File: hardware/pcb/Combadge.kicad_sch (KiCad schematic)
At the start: 21 parts, among them J1 Conn_01x02_Socket, J2 Conn_01x01_Socket, J3 TOUCH, SW1 SW_Push, U1 ESP32-WROOM-32, U2 MAX98357AETE+T

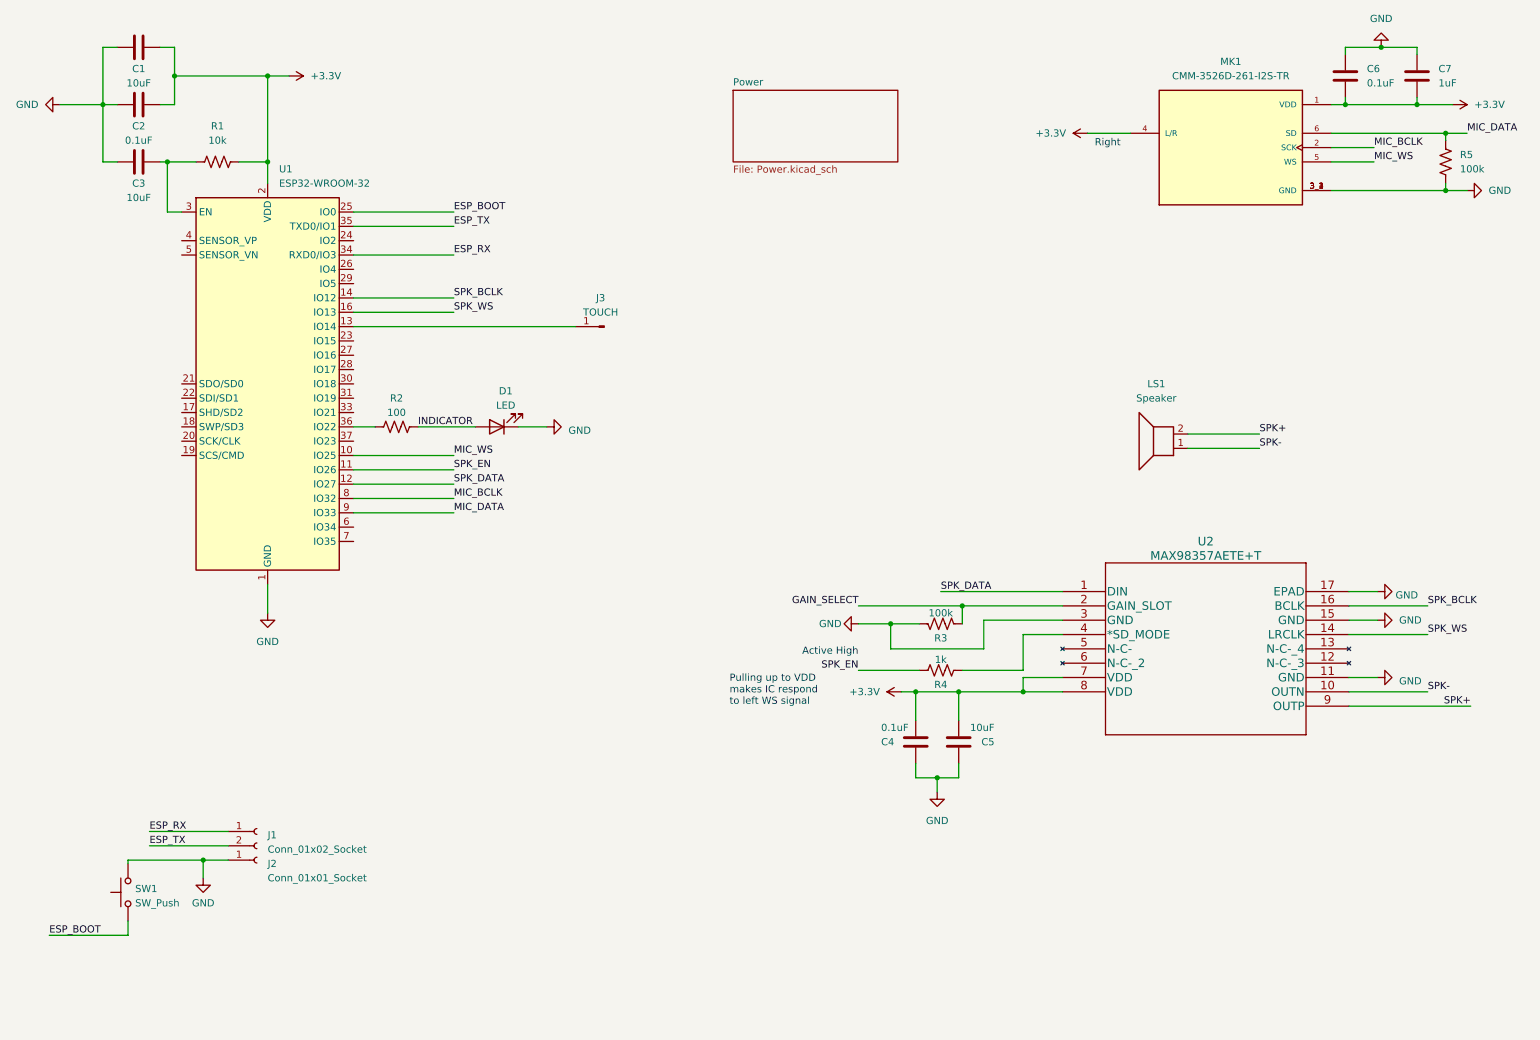
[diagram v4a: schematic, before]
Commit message: Cleanup schematic to follow convention
Thanks to Reddit users Crazy_Direction_1084 and AgentiMi for introducing
me to this.
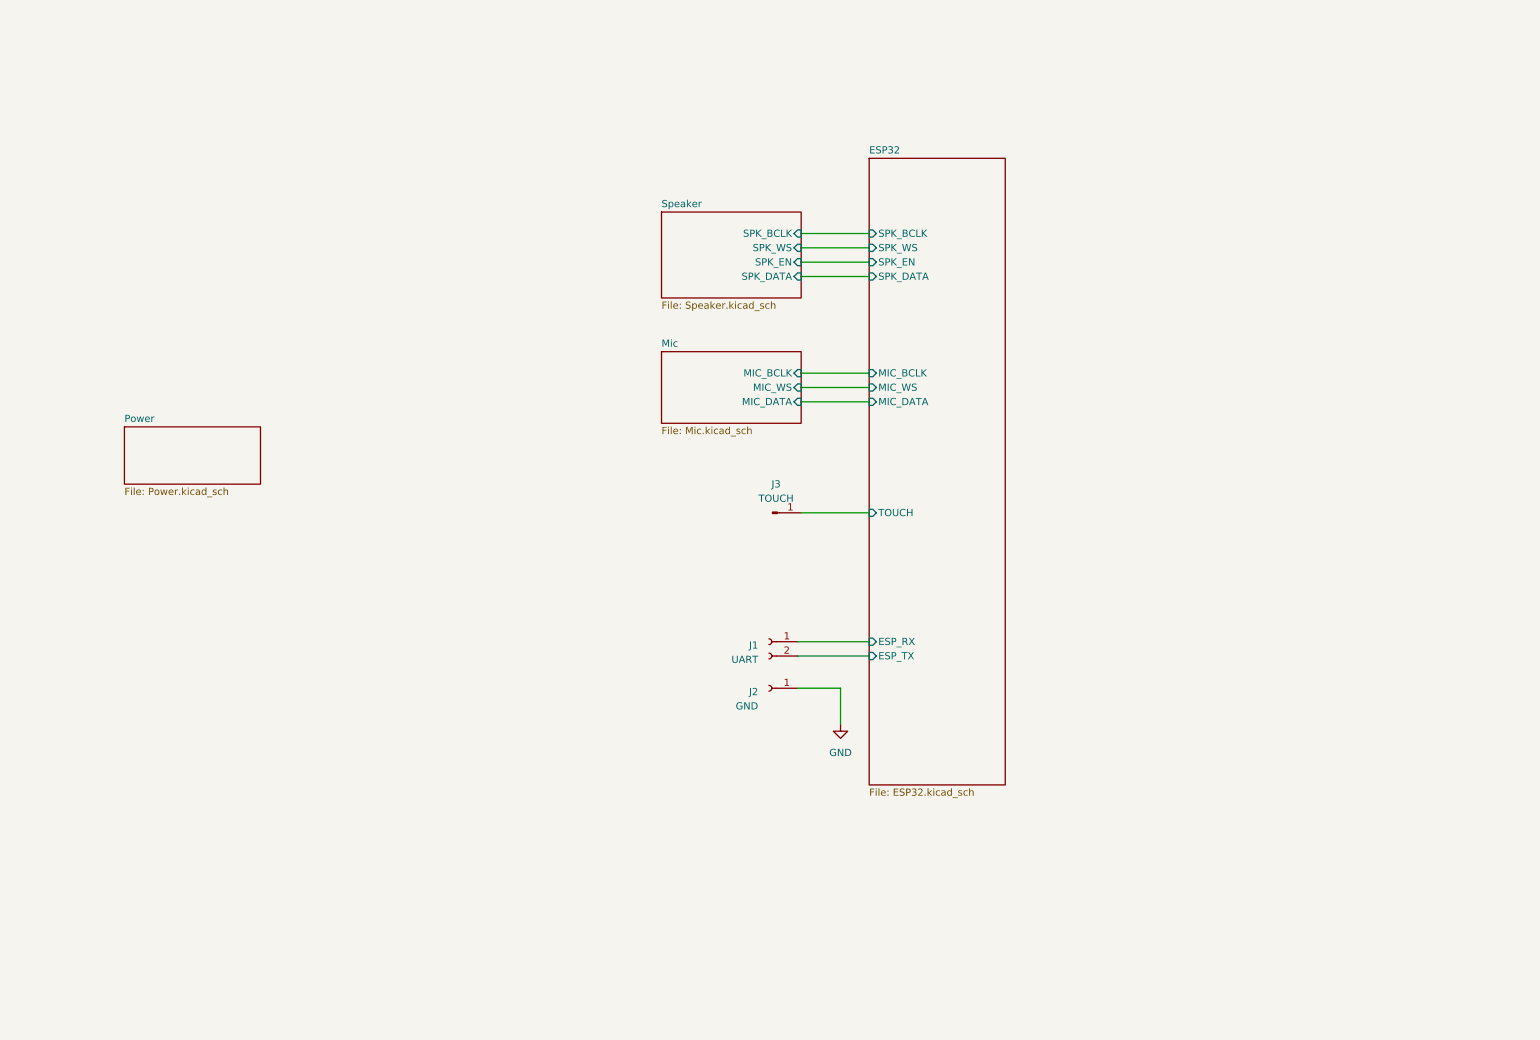
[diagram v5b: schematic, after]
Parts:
- removed C1, C3, C5: 10uF, Capacitor_SMD:C_1206_3216Metric_Pad1.33x1.80mm_HandSolder, symbol Device:C
- removed C2, C4, C6: 0.1uF, Capacitor_SMD:C_1206_3216Metric_Pad1.33x1.80mm_HandSolder, symbol Device:C
- removed C7: 1uF, Capacitor_SMD:C_1206_3216Metric_Pad1.33x1.80mm_HandSolder, symbol Device:C
- removed D1: LED, LED_SMD:LED_0805_2012Metric_Pad1.15x1.40mm_HandSolder, symbol Device:LED
- removed LS1: Speaker, Connector_PinHeader_2.54mm:PinHeader_1x02_P2.54mm_Vertical, symbol Device:Speaker
- removed MK1: CMM-3526D-261-I2S-TR, CMM-3526D-261-I2S-TR:MIC_CMM-3526D-261-I2S-TR, symbol CMM-3526D-261-I2S-TR:CMM-3526D-261-I2S-TR
- removed R1: 10k, Resistor_SMD:R_1206_3216Metric_Pad1.30x1.75mm_HandSolder, symbol Device:R_US
- removed R2: 100, Resistor_SMD:R_1206_3216Metric_Pad1.30x1.75mm_HandSolder, symbol Device:R_US
- removed R3, R5: 100k, Resistor_SMD:R_1206_3216Metric_Pad1.30x1.75mm_HandSolder, symbol Device:R_US
- removed R4: 1k, Resistor_SMD:R_1206_3216Metric_Pad1.30x1.75mm_HandSolder, symbol Device:R_US
- removed SW1: SW_Push, Button_Switch_SMD:SW_SPST_CK_RS282G05A3, symbol Switch:SW_Push
- removed U1: ESP32-WROOM-32, RF_Module:ESP32-WROOM-32, symbol RF_Module:ESP32-WROOM-32
- removed U2: MAX98357AETE+T, MAX98357AETE+T:MAX98357AETE&plus_T, symbol MAX98357AETE+T:MAX98357AETE+T
- J1: value Conn_01x02_Socket -> UART
- J2: value Conn_01x01_Socket -> GND
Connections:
- net ESP32/TOUCH: now reaches J3.1 (Pin_1)
- net ESP_RX renamed ESP32/ESP_RX
- net ESP_TX renamed ESP32/ESP_TX
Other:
- added sheet ESP32 (ESP32.kicad_sch)
- added sheet Mic (Mic.kicad_sch)
- added sheet Speaker (Speaker.kicad_sch)
- note removed: "Active High"
- note removed: "Pulling up to VDD makes IC respond to left WS signal"
- note removed: "Right"
- moved on the sheet: J1, J2

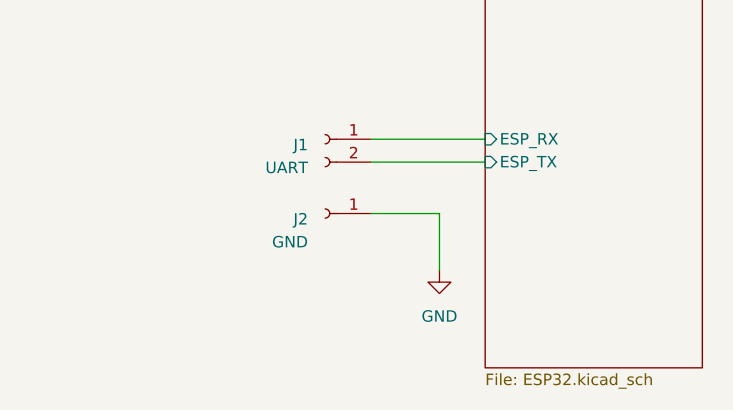
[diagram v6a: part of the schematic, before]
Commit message: Break out ESP enable pin
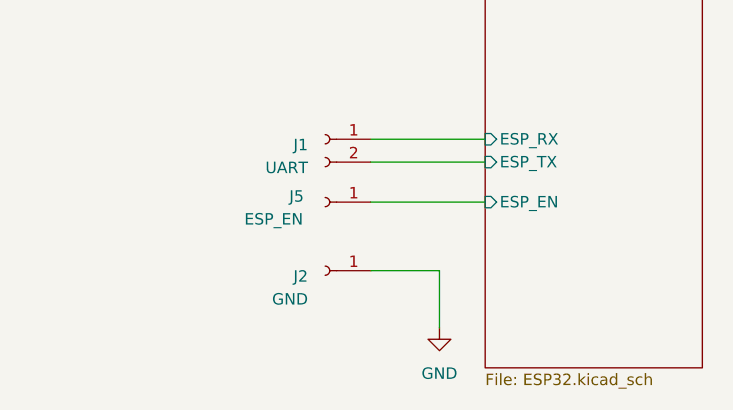
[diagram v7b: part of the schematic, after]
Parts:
- added J5: ESP_EN, Connector_PinHeader_2.54mm:PinHeader_1x01_P2.54mm_Vertical, symbol Connector:Conn_01x01_Socket
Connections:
- new net ESP32/ESP_EN: J5.1 (Pin_1)
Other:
- sheet ESP32 ports: added ESP_EN; removed none
- moved on the sheet: J2
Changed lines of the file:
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@@
     (stroke (width 0) (type default))
   )
-  (wire (pts (xy 161.925 132.715) (xy 161.925 139.065))
+  (wire (pts (xy 154.305 131.445) (xy 167.005 131.445))
+    (stroke (width 0) (type default))
+  )
+  (wire (pts (xy 161.925 139.065) (xy 161.925 145.415))
     (stroke (width 0) (type default))
   )
@@
     (stroke (width 0) (type default))
   )
-  (wire (pts (xy 154.305 132.715) (xy 161.925 132.715))
+  (wire (pts (xy 154.305 139.065) (xy 161.925 139.065))
     (stroke (width 0) (type default))
   )
@@
     )
   )
-  (symbol (lib_id "power:GND") (at 161.925 139.065 0) (unit 1)
+  (symbol (lib_id "Connector:Conn_01x01_Socket") (at 149.225 131.445 180) (unit 1)
+    (in_bom yes) (on_board yes) (dnp no)
+    (property "Reference" "J5" (at 146.05 130.81 0)
+      (effects (font (size 1.27 1.27)))
+    )
+    (property "Value" "ESP_EN" (at 143.51 133.35 0)
+      (effects (font (size 1.27 1.27)))
+    )
+    (property "Footprint" "Connector_PinHeader_2.54mm:PinHeader_1x01_P2.54mm_Vertical" (at 149.225 131.445 0)
+      (effects (font (size 1.27 1.27)) hide)
+    )
+    (property "Datasheet" "~" (at 149.225 131.445 0)
+      (effects (font (size 1.27 1.27)) hide)
+    )
+    (pin "1")
+    (instances
+      (project "Combadge"
+        (path "/dc42e7bc-f663-434d-8744-232038ac4fdf"
+          (reference "J5") (unit 1)
+        )
+      )
+    )
+  )
+  (symbol (lib_id "power:GND") (at 161.925 145.415 0) (unit 1)
     (in_bom yes) (on_board yes) (dnp no) (fields_autoplaced)
-    (property "Reference" "#PWR01" (at 161.925 145.415 0)
-      (effects (font (size 1.27 1.27)) hide)
-    )
-    (property "Value" "GND" (at 161.925 144.145 0)
-      (effects (font (size 1.27 1.27)))
-    )
-    (property "Footprint" "" (at 161.925 139.065 0)
-      (effects (font (size 1.27 1.27)) hide)
-    )
-    (property "Datasheet" "" (at 161.925 139.065 0)
+    (property "Reference" "#PWR01" (at 161.925 151.765 0)
+      (effects (font (size 1.27 1.27)) hide)
+    )
+    (property "Value" "GND" (at 161.925 150.495 0)
+      (effects (font (size 1.27 1.27)))
+    )
+    (property "Footprint" "" (at 161.925 145.415 0)
+      (effects (font (size 1.27 1.27)) hide)
+    )
+    (property "Datasheet" "" (at 161.925 145.415 0)
       (effects (font (size 1.27 1.27)) hide)
     )
@@
     )
   )
-  (symbol (lib_id "Connector:Conn_01x01_Socket") (at 149.225 132.715 0) (mirror y) (unit 1)
+  (symbol (lib_id "Connector:Conn_01x01_Socket") (at 149.225 139.065 0) (mirror y) (unit 1)
     (in_bom yes) (on_board yes) (dnp no)
-    (property "Reference" "J2" (at 147.32 133.35 0)
-      (effects (font (size 1.27 1.27)) (justify left))
-    )
-    (property "Value" "GND" (at 147.32 135.89 0)
-      (effects (font (size 1.27 1.27)) (justify left))
-    )
-    (property "Footprint" "Connector_PinHeader_2.54mm:PinHeader_1x01_P2.54mm_Vertical" (at 149.225 132.715 0)
-      (effects (font (size 1.27 1.27)) hide)
-    )
-    (property "Datasheet" "~" (at 149.225 132.715 0)
+    (property "Reference" "J2" (at 147.32 139.7 0)
+      (effects (font (size 1.27 1.27)) (justify left))
+    )
+    (property "Value" "GND" (at 147.32 142.24 0)
+      (effects (font (size 1.27 1.27)) (justify left))
+    )
+    (property "Footprint" "Connector_PinHeader_2.54mm:PinHeader_1x01_P2.54mm_Vertical" (at 149.225 139.065 0)
+      (effects (font (size 1.27 1.27)) hide)
+    )
+    (property "Datasheet" "~" (at 149.225 139.065 0)
       (effects (font (size 1.27 1.27)) hide)
     )
@@
       (effects (font (size 1.27 1.27)) (justify left))
     )
+    (pin "ESP_EN" input (at 167.005 131.445 180)
+      (effects (font (size 1.27 1.27)) (justify left))
+    )

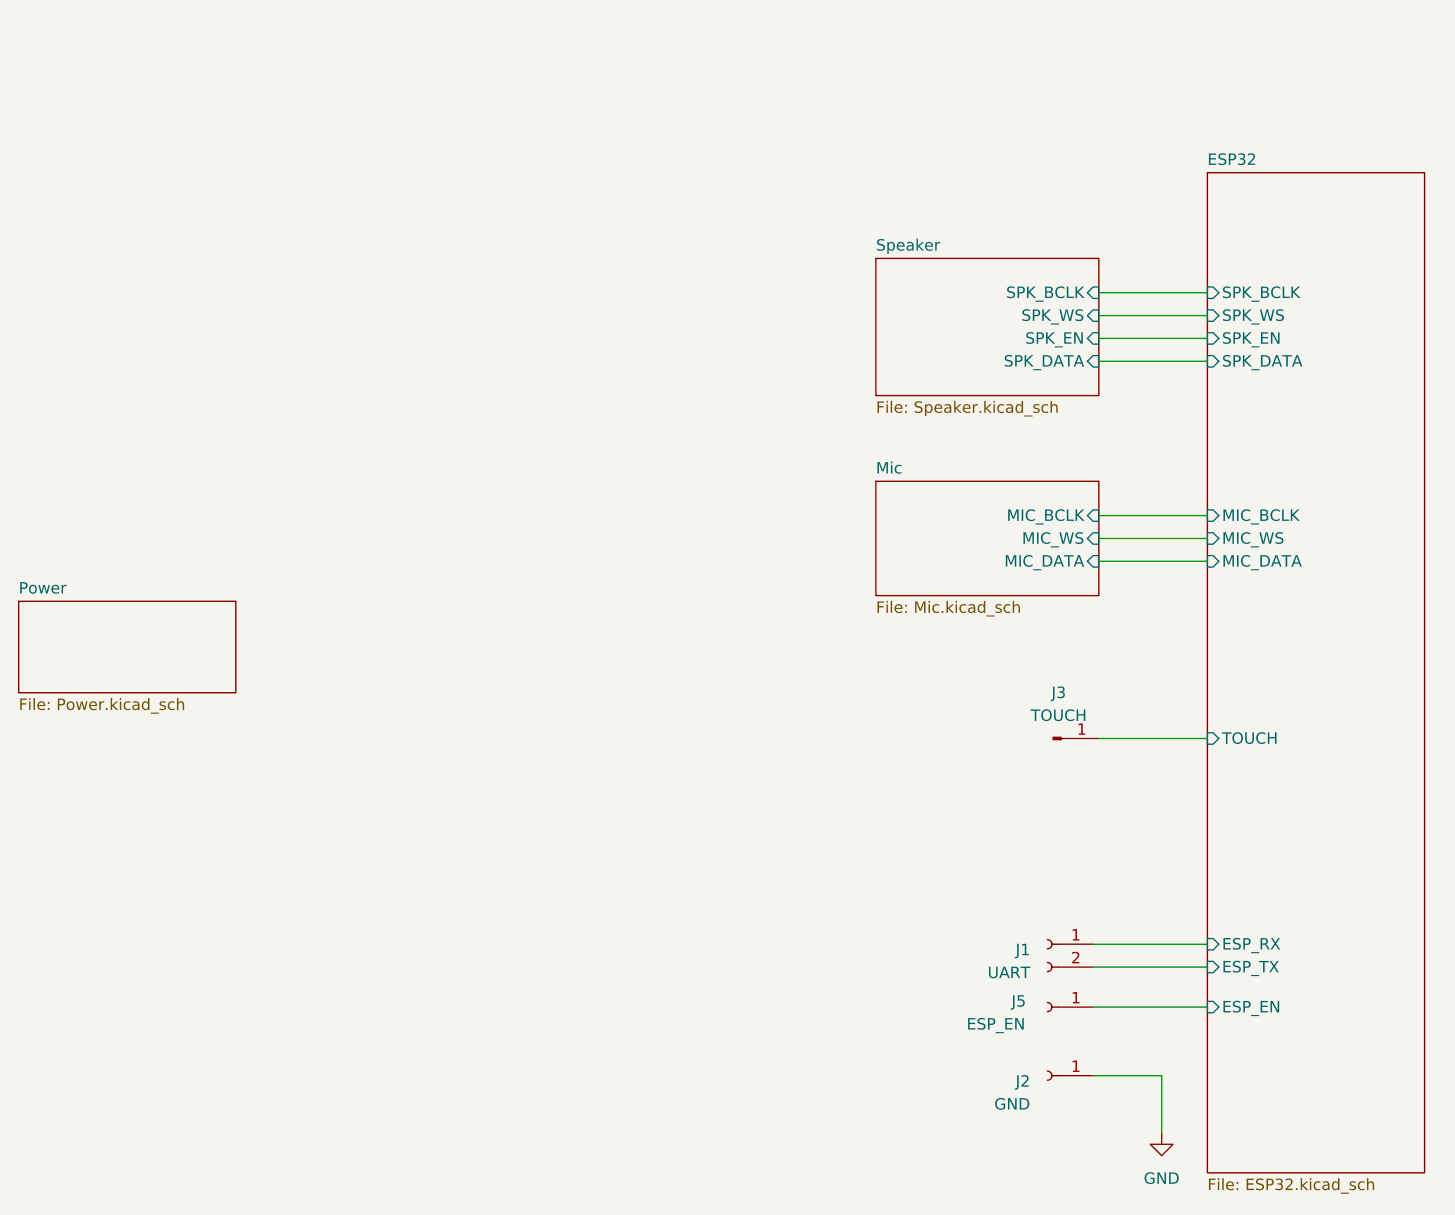
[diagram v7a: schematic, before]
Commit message: Replace ESP32 with ESP32-S3
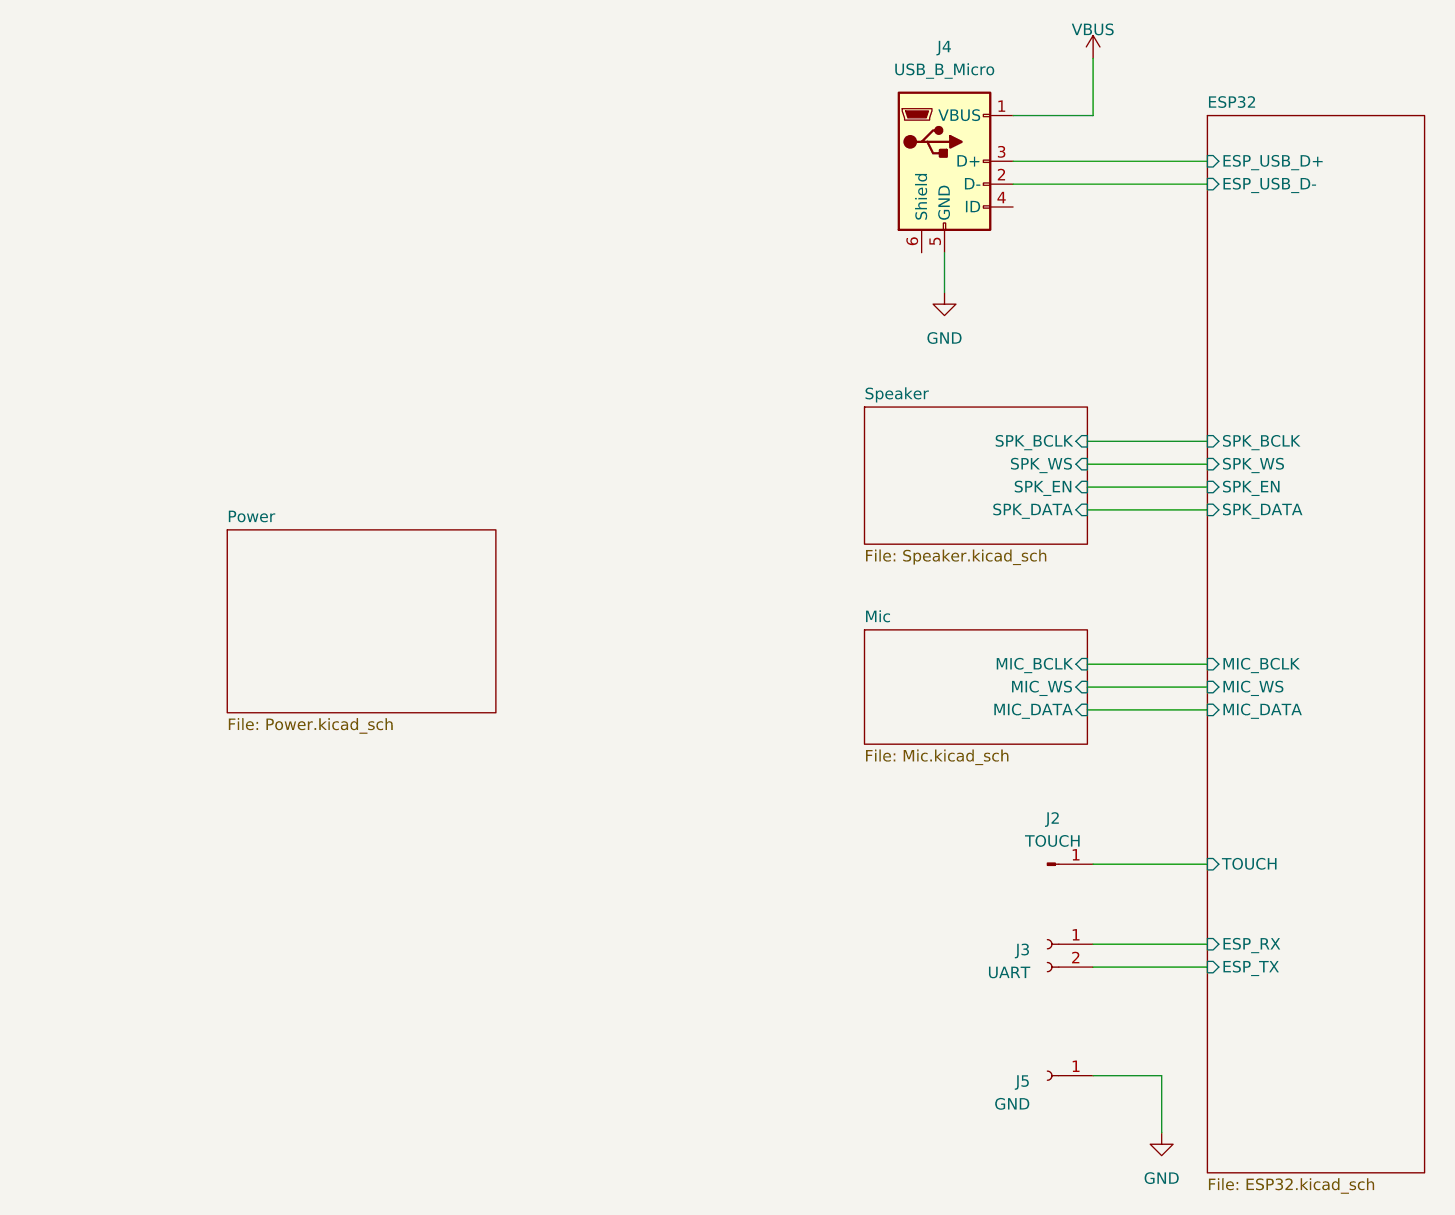
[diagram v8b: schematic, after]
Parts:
- removed J5: ESP_EN, Connector_PinHeader_2.54mm:PinHeader_1x01_P2.54mm_Vertical, symbol Connector:Conn_01x01_Socket
- added J4: USB_B_Micro, Connector_USB:USB_Micro-B_Amphenol_10118194_Horizontal, symbol Connector:USB_B_Micro
- renumbered J3 to J2, J1 to J3, J2 to J5
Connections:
- net GND: now also J4.5 (GND)
- new net ESP32/ESP_USB_D+: J4.3 (D+)
- new net ESP32/ESP_USB_D-: J4.2 (D-)
- new net VBUS: J4.1 (VBUS)
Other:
- sheet ESP32 ports: added ESP_USB_D+, ESP_USB_D-; removed ESP_EN
- moved on the sheet: J2
